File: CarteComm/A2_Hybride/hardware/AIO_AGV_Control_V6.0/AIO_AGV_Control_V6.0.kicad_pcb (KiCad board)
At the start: 2 copper layers, 58 parts, among them J1 DB25_Pins, J2 DB25_Socket, T1 IRF520, T10 IRF520, T11 IRF520, T12 IRF520, T14 IRF520, T15 IRF520, T16 IRF520, T17 IRF520, T18 IRF520, T19 IRF520, T2 IRF520, T20 IRF520, T21 IRF520, T22 IRF520, T23 IRF520, T24 IRF520, T3 IRF520, T4 IRF520, T5 IRF520, T6 IRF520, T7 IRF520, T8 IRF520, T9 IRF520, U1 ESP32-DEVKITC, U2 RFM95W-868S2

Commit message: feat(lora): remplacer la passerelle MQTT par une passerelle LoRa dans A2 et A3
Vous aviez raison de relever l'incohérence : ces deux architectures n'ont ni
broker, ni réseau d'entreprise, et leur firmware ESP32 portait pourtant un
GatewayApp qui publiait sur des topics et dépendait d'IMqttPublisher. Je l'avais
laissé en dette plutôt que de l'écrire.

LoraGatewayApp le remplace. Il rend exactement le même service côté ATmega -
mêmes trames de liaison, même heartbeat, même repli de sécurité - et change
seulement la source des ordres : trames applicatives de 9 octets sur ITransport,
accusé renvoyé par la même voie, idempotence (node_id, seq) en table locale.

Le budget de rapport cyclique s'applique aussi aux accusés, parce qu'un
récepteur qui acquitte est un émetteur. Un accusé refusé faute de budget est
compté, pas perdu en silence.

Le firmware ESP32 est réécrit : plus de Wi-Fi STA ni de client MQTT, mais SPI +
Sx1276Radio + LoraTransport, avec le brochage relevé sur votre V6.0 dans
board_pins.h - IO5, IO18, IO19, IO23, IO26, et kLoraReset à 0xFF puisque la
broche RESET du RFM95W n'est pas connectée au PCB.

MqttConfig et WifiConfig quittent le profil, la section lora: y entre, et
aes_enabled passe à true : sans TLS, le chiffrement applicatif est la seule
protection de la liaison radio. Le champ mqtt_up de /agvdump est conservé
volontairement - c'est un contrat d'atelier, il porte désormais l'état radio.

Deux défauts trouvés en écrivant les tests, et corrigés. La détection de silence
de l'ATmega utilisait 0 comme sentinelle « jamais reçu », alors que c'est un
instant valide au démarrage. Et surtout, les quatre Makefile ne suivaient pas
les dépendances d'en-têtes : modifier une classe ne recompilait pas ses
utilisateurs, on reliait des objets compilés contre deux versions de la même
classe, et un test échouait sans qu'aucune erreur ne soit signalée. -MMD -MP
partout.

Kanban LG1 soldé. 470 tests verts, dont 10 nouveaux sur la passerelle.

Co-Authored-By: Claude Opus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
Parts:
- added J3: Conn_Coaxial_Small, Connector_Coaxial:SMA_Amphenol_901-143_Horizontal, F.Cu at (59.0, 89.8)
- moved LM1 27.1 mm to (153.6, 151.8)
- moved R40 27.1 mm to (138.8, 147.8)
- moved T18 27.1 mm to (129.4, 52.8)
- moved T10 27.1 mm to (87.8, 69.2)
- moved A1 27.1 mm to (114.7, 145.2)
- moved D1 27.1 mm to (177.1, 117.8)
- moved J1 27.1 mm to (126.2, 37.5)
- moved J2 27.1 mm to (184.3, 131.6)
- moved R1 27.1 mm to (176.5, 75.2)
- moved R10 27.1 mm to (94.5, 75.3)
- moved R11 27.1 mm to (85.5, 75.3)
- moved R12 27.1 mm to (76.5, 75.3)
- moved R14 27.1 mm to (172.0, 59.4)
- moved R15 27.1 mm to (163.0, 59.4)
- moved R16 27.1 mm to (154.0, 59.4)
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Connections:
- U2 pad 10: unconnected-(U2-GND-Pad10) -> Net-(J3-Ext)
- U2 pad 9: unconnected-(U2-ANT-Pad9) -> Net-(J3-In)
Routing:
- net Net-(J3-Ext): track 0.00 -> 24.9 mm
- net Net-(J3-In): track 0.00 -> 9.01 mm

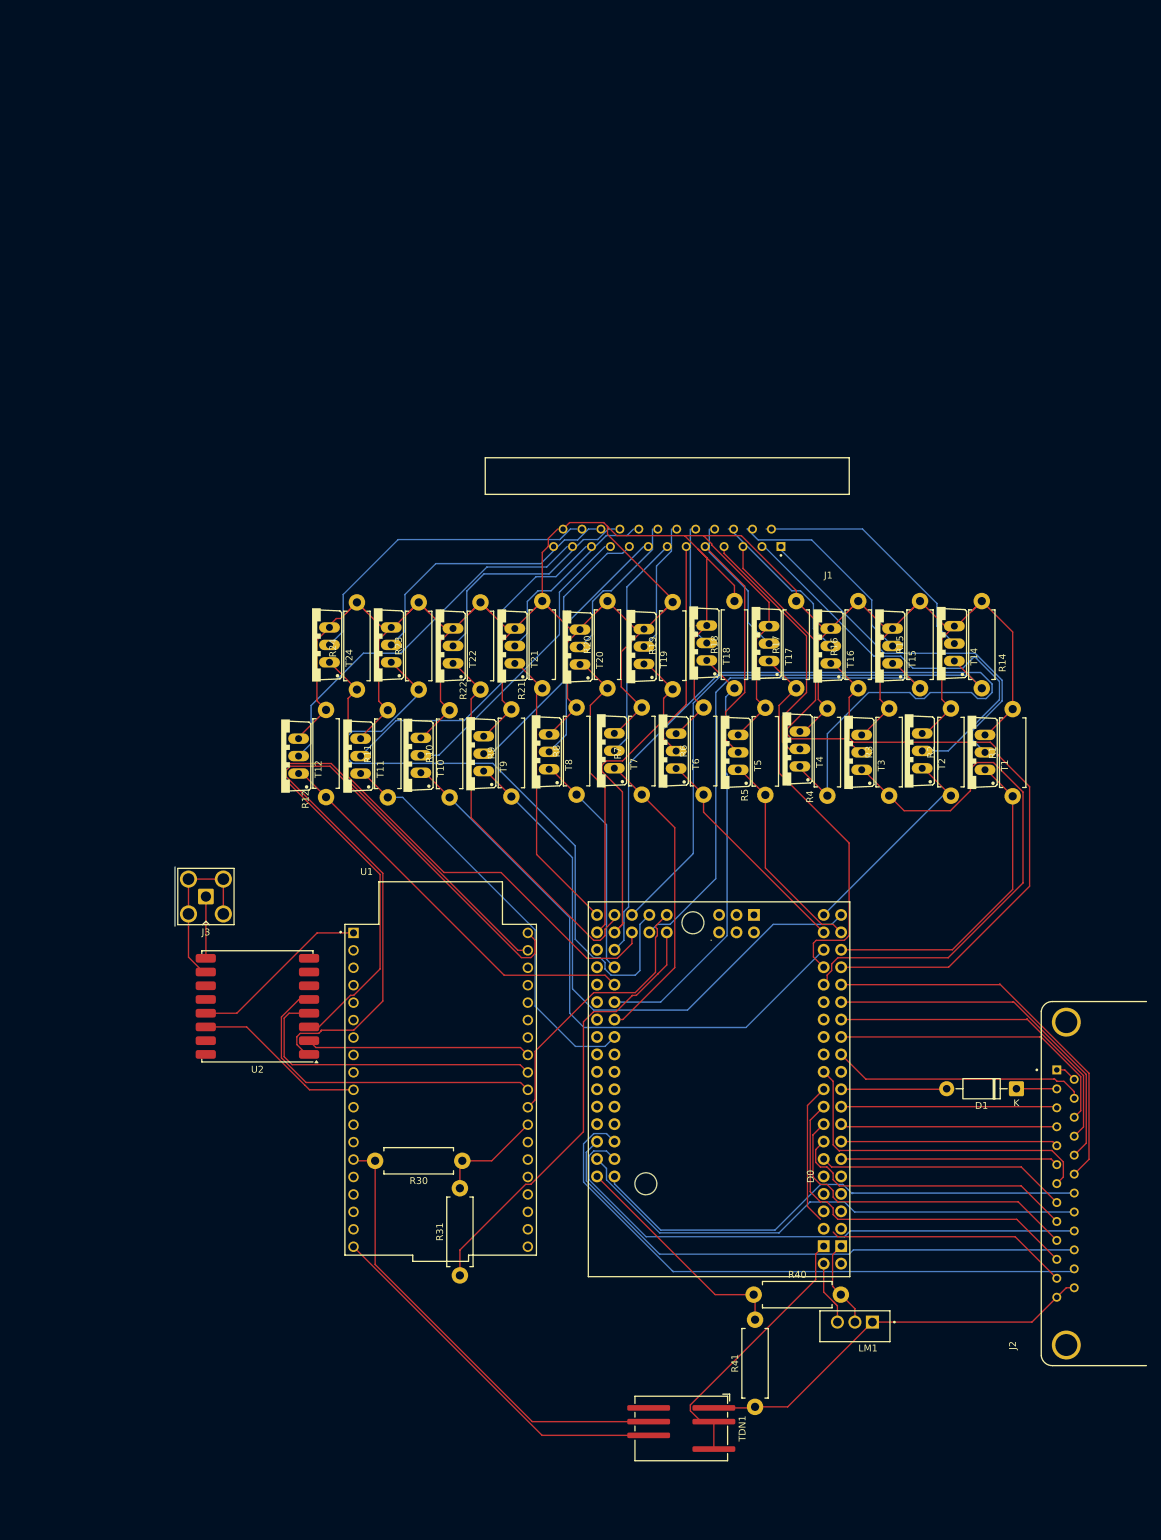
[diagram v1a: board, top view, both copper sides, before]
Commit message: feat(banc): banc d'essai des boutons EnOcean pour UniPi E413
Service web qui enregistre les PTM 210, les détecte à l'appui ou par saisie de
l'identifiant, et ouvre une fenêtre verte à chaque pression avec le nom, le
code, l'heure et le niveau reçu.

Deux règles font la différence entre un banc utilisable et un banc qui ment. Un
PTM 210 émet TROIS sous-télégrammes par appui, et émet aussi au relâchement :
sans traitement, une pression afficherait six fenêtres. Le banc déduplique sur
(identifiant, données) dans une fenêtre de 400 ms et ne retient que le front
d'appui. Deux tests vérifient précisément cela.

Un appui non enregistré ouvre une fenêtre ambre au lieu d'être ignoré : au banc,
c'est exactement ce qu'on cherche à voir.

L'ajout par détection couvre les deux gestes réels. On peut armer la fenêtre
puis presser, mais on peut aussi avoir pressé AVANT d'ouvrir la boîte de
dialogue - le dernier appui capté est alors proposé, ce qui évite de faire le
tour de l'atelier deux fois.

Les identifiants se lisent en hexadécimal sans exception, y compris pour une
chaîne de chiffres seuls : 2732996 est un hexadécimal valide, et deviner entre
les deux bases produirait un identifiant faux une fois sur deux.

Bibliothèque standard seule hors pyserial, flux SSE, registre JSON lisible à la
main, port série détecté par lien by-id plutôt que par ttyUSB0 dont le numéro
change au rebranchement. Un mode simulation permet de tout éprouver sans
matériel.

Le banc ne dépend d'aucun dossier d'architecture : il sert à valider les boutons
avant que le choix ne soit tranché, et vaut pour A1, A2 et A4. Le décodeur ESP3
y est copié, avec la note de report réciproque.

17 tests, unité systemd durcie, README de déploiement.

Co-Authored-By: Claude Opus 5 <noreply@anthropic.com>
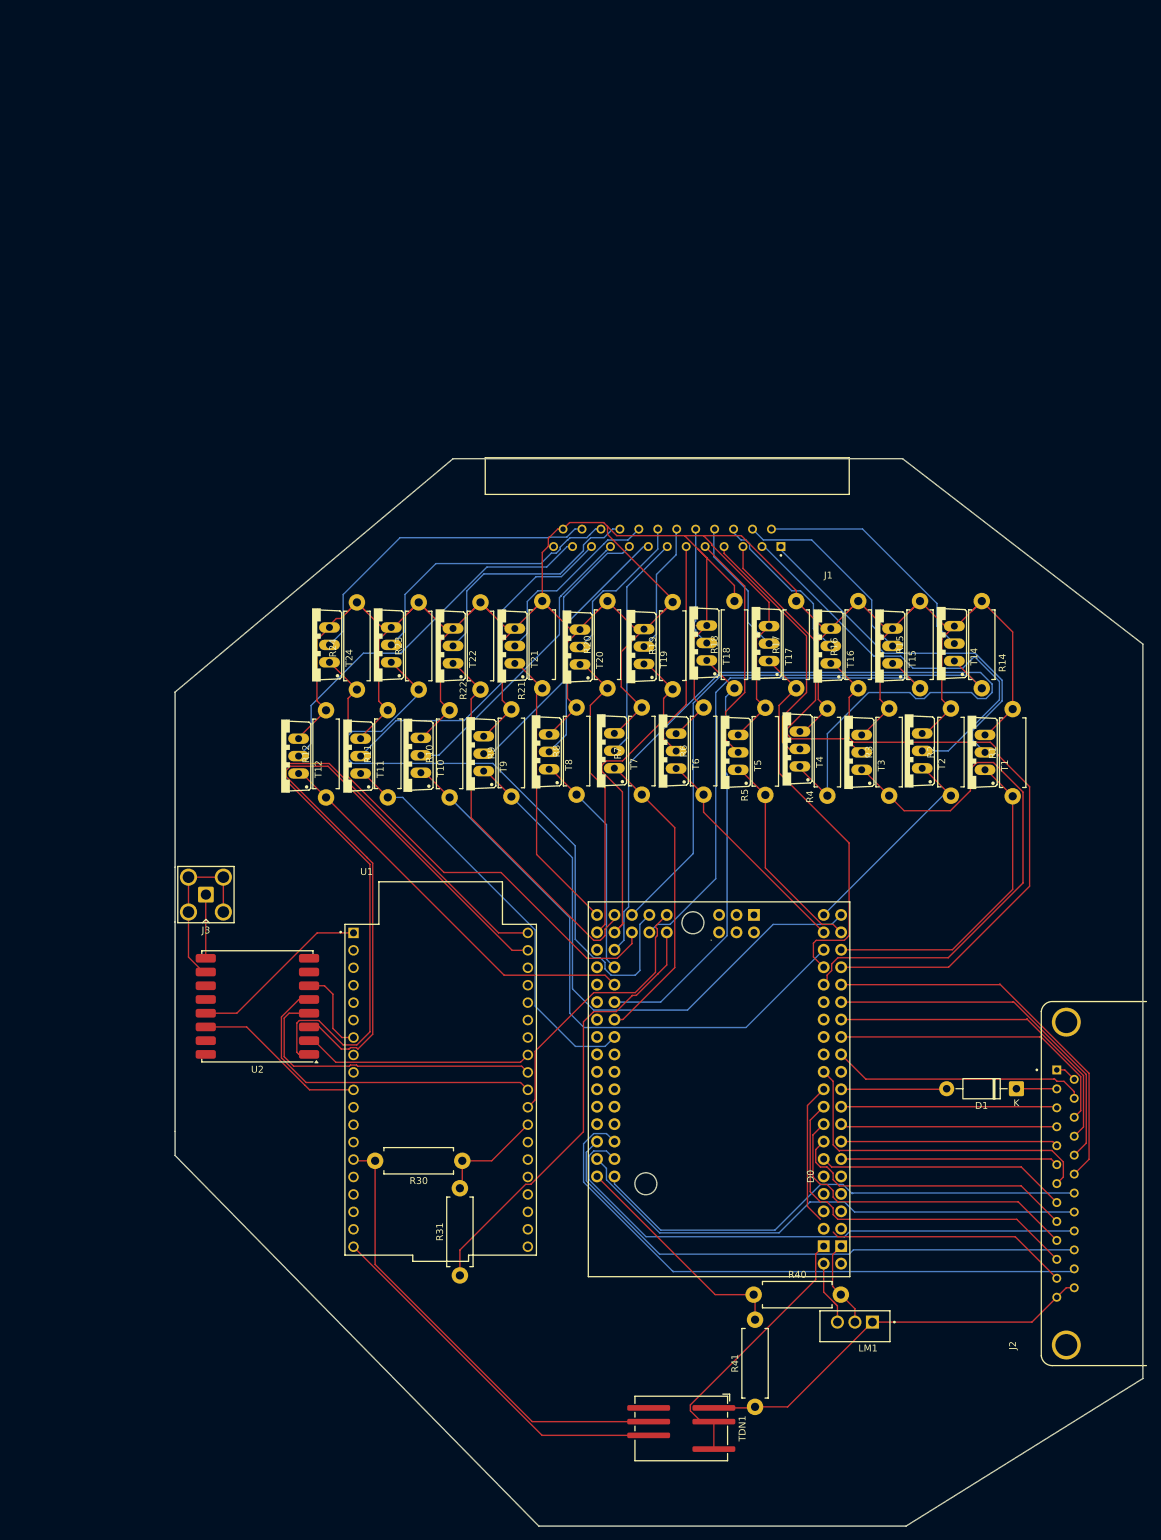
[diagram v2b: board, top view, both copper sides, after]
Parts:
- moved J3 0.28 mm to (59.0, 89.5)
- moved R12 0.05 mm to (76.5, 75.3)
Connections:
- U2 pad 6: unconnected-(U2-RESET-Pad6) -> unconnected-(U1-IO32-Pad7)
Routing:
- net unconnected-(U1-IO32-Pad7): track 0.00 -> 12.5 mm
- net Net-(U1-IO23): track 96.0 -> 102.0 mm
- net Net-(J1-P23): track 40.0 -> 41.7 mm
- net Net-(J1-P15): track 31.3 -> 29.6 mm
- net Net-(J1-P22): track 34.1 -> 35.4 mm
- net Net-(U1-IO19): track 32.7 -> 33.6 mm
- net Net-(J1-P25): track 475.2 -> 475.9 mm
- net Net-(J1-P24): track 46.1 -> 46.9 mm
- net Net-(J1-Pad12): track 55.0 -> 55.8 mm
- net Net-(J1-Pad11): track 51.6 -> 52.4 mm
- net Net-(J1-P21): track 27.1 -> 27.9 mm
- net Net-(J1-P14): track 37.2 -> 36.4 mm
- net Net-(J1-P20): track 22.2 -> 23.0 mm
- net Net-(U1-GND3): track 109.5 -> 108.9 mm
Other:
- board outline added: 141 x 155.5 mm
